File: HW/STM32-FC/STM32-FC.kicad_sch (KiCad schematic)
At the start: 39 parts, among them J1 GH 1.25mm 6P, Q1 S9013, SW2 SW_DIP_x03, U1 STM32F407VETx, Y1 16MHz

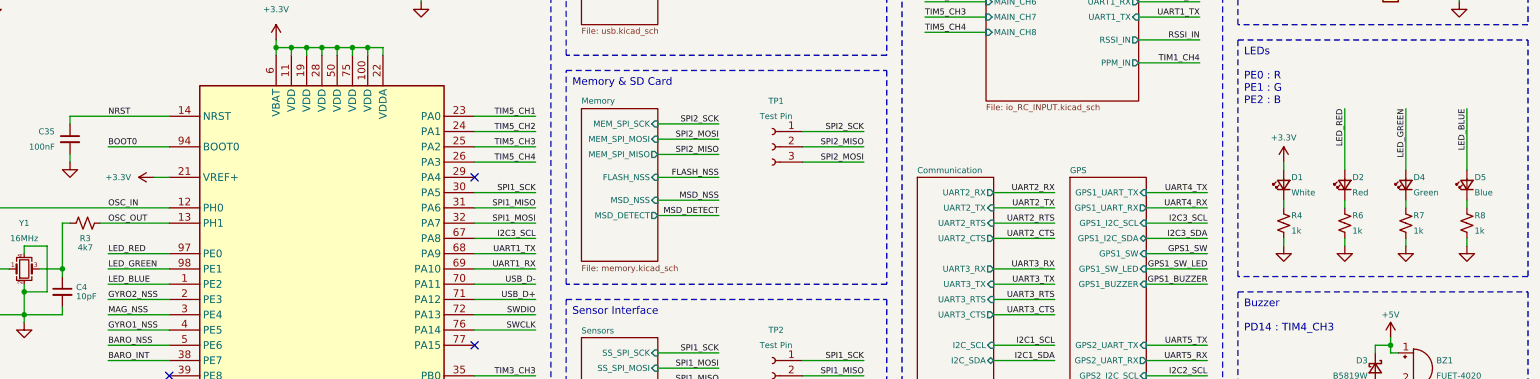
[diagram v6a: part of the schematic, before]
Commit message: 2025.02.07 USB C Conn change v1
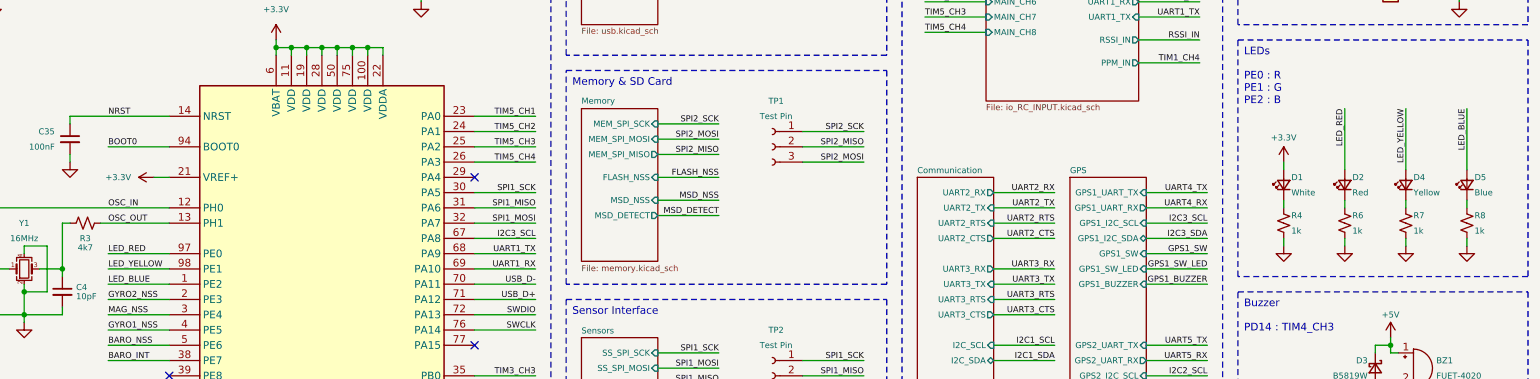
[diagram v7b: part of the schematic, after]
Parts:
- C10, C12, C3, C35, C7, C8, C9: LCSC C1581 -> C1525
- C11: LCSC C1926 -> C14445
- C2: LCSC C40894 -> C77000
- C5, C6: LCSC C1950 -> C170151
- D4: value Green -> Yellow; LCSC C130723 -> C130721
- J1: LCSC C19626244 -> C133065
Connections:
- net LED_GREEN renamed LED_YELLOW
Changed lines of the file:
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@@
 		)
 	)
-	(label "LED_GREEN"
+	(label "LED_YELLOW"
 		(at 264.16 52.07 270)
 		(effects
@@
 		)
 	)
-	(label "LED_GREEN"
+	(label "LED_YELLOW"
 		(at 48.26 78.74 0)
 		(effects
@@
 			)
 		)
-		(property "LCSC" "C1950 "
+		(property "LCSC" "C170151"
 			(at 41.91 168.91 0)
 			(effects
@@
 			)
 		)
-		(property "LCSC" "C1581"
+		(property "LCSC" "C1525"
 			(at 39.37 55.8862 0)
 			(effects
@@
 			)
 		)
-		(property "LCSC" "C40894"
+		(property "LCSC" "C77000"
 			(at 31.75 27.9462 0)
 			(effects
@@
 			)
 		)
-		(property "Value" "Green"
+		(property "Value" "Yellow"
 			(at 265.43 66.04 90)
 			(effects
@@
 			)
 		)
-		(property "LCSC" "C130723"
+		(property "LCSC" "C130721"
 			(at 264.16 64.77 0)
 			(effects
@@
 			)
 		)
-		(property "LCSC" "C1926"
+		(property "LCSC" "C14445"
 			(at 102.87 27.9462 0)
 			(effects
@@
 			)
 		)
-		(property "LCSC" "C1581"
+		(property "LCSC" "C1525"
 			(at 43.18 27.9462 0)
 			(effects
@@
 			)
 		)
-		(property "LCSC" "C1950 "
+		(property "LCSC" "C170151"
 			(at 46.99 168.91 0)
 			(effects
@@
 			)
 		)
-		(property "LCSC" "C1581"
+		(property "LCSC" "C1525"
 			(at 66.04 27.9462 0)
 			(effects
@@
 			)
 		)
-		(property "LCSC" "C1581"
+		(property "LCSC" "C1525"
 			(at 54.61 27.9462 0)
 			(effects
@@
 			)
 		)
-		(property "LCSC" "C1581"
+		(property "LCSC" "C1525"
 			(at 111.76 27.9462 0)
 			(effects
@@
 			)
 		)
-		(property "LCSC" "C1581"
+		(property "LCSC" "C1525"
 			(at 77.47 27.9462 0)
 			(effects
@@
 			)
 		)
-		(property "LCSC" "C19626244 "
+		(property "LCSC" "C133065"
 			(at 261.62 25.4 0)
 			(effects
@@
 			)
 		)
-		(property "LCSC" "C1581"
+		(property "LCSC" "C1525"
 			(at 88.9 27.9462 0)
 			(effects

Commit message: 2025.02.11 PCB DONE! MEMO UPDATING
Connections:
- net TIM1_CH4 renamed PPM_IN
- net UART1_RX renamed DSM/SBUS
- net UART1_TX renamed SRXL2
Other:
- note added: "SWDIO : PA13 SWCLK : PA14 NRST : NRST(14)"
- note added: "W : PWR R : PE0 Y : PE1 B : PE2"
- note removed: "PA13 : SWDIO PA14 : SWCLK"
- note removed: "PE0 : R PE1 : G PE2 : B"
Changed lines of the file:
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@@
 	(title_block
 		(title "STM32 Flight Controller")
-		(date "2025-02-05")
+		(date "2025-02-08")
 		(rev "A")
 		(company "NARAE")
@@
 		)
 	)
-	(text "PE0 : R\nPE1 : G\nPE2 : B"
+	(text "W : PWR\nR : PE0\nY : PE1\nB : PE2"
 		(exclude_from_sim no)
 		(at 237.236 45.974 0)
@@
 		)
 	)
-	(text "PA13 : SWDIO\nPA14 : SWCLK"
+	(text "SWDIO : PA13\nSWCLK : PA14\nNRST  : NRST(14)"
 		(exclude_from_sim no)
 		(at 237.236 18.034 0)
@@
 		)
 	)
-	(label "UART1_TX"
+	(label "SRXL2"
 		(at 229.87 36.83 180)
 		(effects
@@
 		)
 	)
-	(label "UART1_RX"
+	(label "DSM{slash}SBUS"
 		(at 229.87 34.29 180)
 		(effects
@@
 		)
 	)
-	(label "UART1_TX"
+	(label "SRXL2"
 		(at 119.38 76.2 180)
 		(effects
@@
 		)
 	)
-	(label "UART1_RX"
+	(label "DSM{slash}SBUS"
 		(at 119.38 78.74 180)
 		(effects
@@
 		)
 	)
-	(label "TIM1_CH4"
+	(label "PPM_IN"
 		(at 229.87 44.45 180)
 		(effects
@@
 		)
 	)
-	(label "TIM1_CH4"
+	(label "PPM_IN"
 		(at 48.26 111.76 0)
 		(effects
